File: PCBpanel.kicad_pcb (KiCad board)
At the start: 2 copper layers, 100 x 100.2 mm, 93 parts, among them P1 CONN_01X05, P1 CONN_01X13, P1 CONN_buzz, P2 CONN_01X03, P2 CONN_01X09, P3 CONN_01X04, P3 CONN_01X09, P3 CONN_01X13, P4 CONN_01X02, Q1 BSS138, Q1 BSS84, Q1 NPN, Q2 BSS138, SW1 SW_PUSH, U1 ESP-12E, U1 GY-NEO6MV2, U2 AP1117, U3 ESP8266_THING, U4 MPU6050, U5 NVSRAM, U6 BMP180, U7 HTU21D

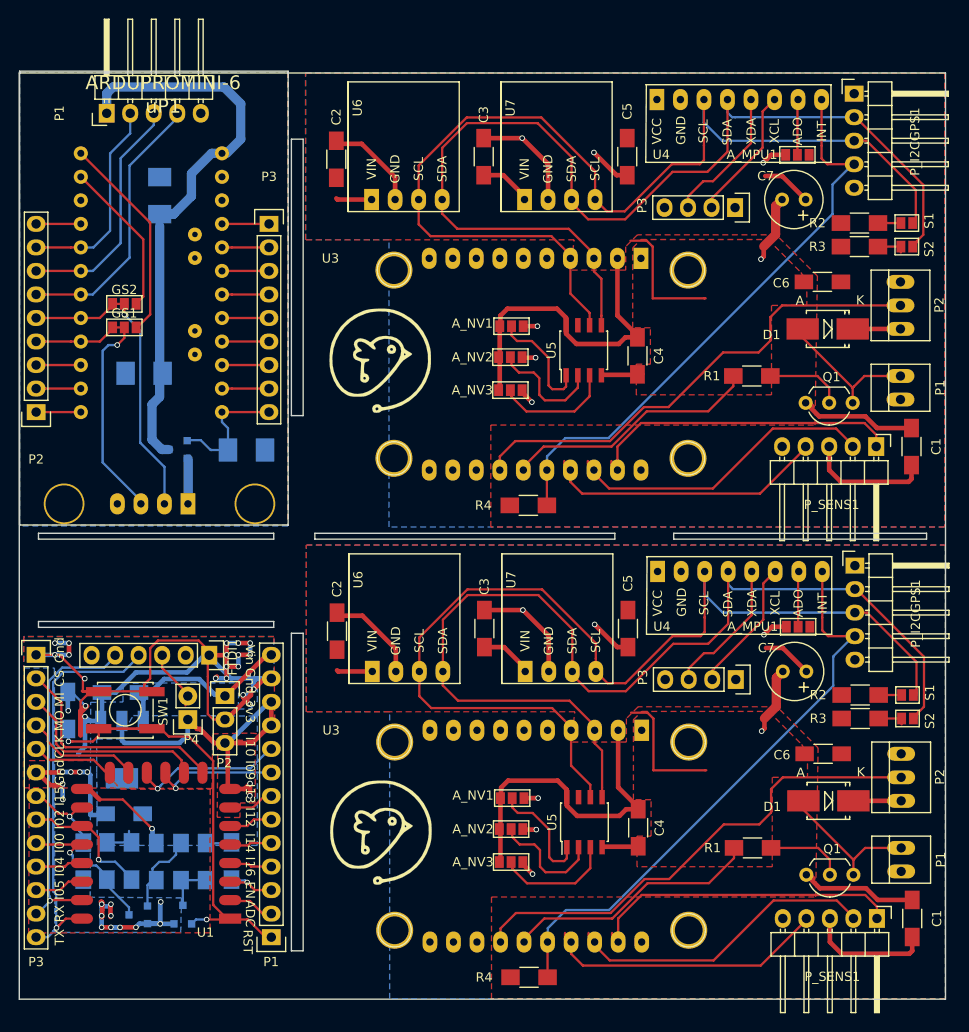
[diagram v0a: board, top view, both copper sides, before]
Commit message: alfa prototype
updated for first pcb prototype
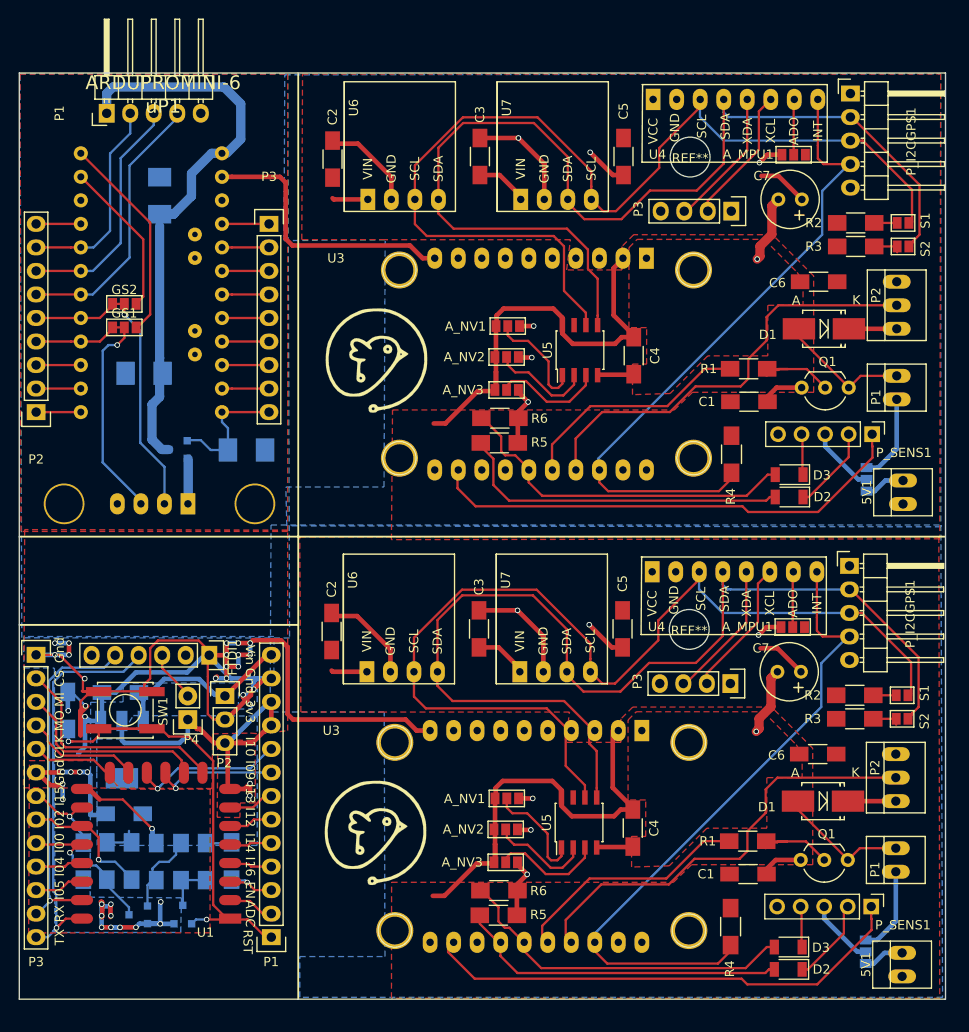
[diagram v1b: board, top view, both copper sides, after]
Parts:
- removed the A_MPU1 at (134.0, 58.8)
- removed the A_MPU1 at (134.1, 109.8)
- removed the A_NV1 at (103.1, 77.3)
- removed the A_NV1 at (103.2, 128.3)
- removed the A_NV2 at (103.0, 80.7)
- removed the A_NV2 at (103.1, 131.6)
- removed the A_NV3 at (103.0, 84.2)
- removed the A_NV3 at (103.1, 135.2)
- removed the C1 at (146.3, 90.3)
- removed the C1 at (146.4, 141.3)
- removed the C2 at (84.2, 59.3)
- removed the C2 at (84.3, 110.3)
- removed the C3 at (100.1, 59.0)
- removed the C3 at (100.2, 110.0)
- removed the C4 at (116.7, 80.5)
- removed the C4 at (116.8, 131.5)
- removed the C5 at (115.6, 59.0)
- removed the C5 at (115.7, 110.0)
- removed the C6 at (136.7, 72.6)
- removed the C6 at (136.8, 123.5)
- removed the C7 at (134.9, 63.7)
- removed the C7 at (135.0, 114.6)
- removed the D1 at (137.3, 77.6)
- removed the D1 at (137.4, 128.6)
- removed G*** (x2): LOGO, Adem_Kicad_logos:adem_logo
- removed G*** (x2): LOGO, Adem_Kicad_logos:adem_logo-txt_17_B_silk
- removed the P1 at (145.1, 84.0)
- removed the P1 at (145.2, 134.9)
- removed the P2 at (145.1, 75.1)
- removed the P2 at (145.2, 126.0)
- removed the P3 at (127.3, 64.5)
- removed the P3 at (127.4, 115.5)
- removed the P_I2CGPS1 at (140.1, 52.2)
- removed the P_I2CGPS1 at (140.2, 103.2)
- removed the P_SENS1 at (142.5, 90.3)
- removed the P_SENS1 at (142.6, 141.3)
- removed the Q1 at (140.0, 85.6)
- removed the Q1 at (140.1, 136.6)
- removed the R1 at (129.1, 82.7)
- removed the R1 at (129.2, 133.7)
- removed the R2 at (140.7, 66.2)
- removed the R2 at (140.8, 117.2)
- removed the R3 at (140.7, 68.7)
- removed the R3 at (140.8, 119.7)
- removed the R4 at (105.0, 96.7)
- removed the R4 at (105.0, 147.6)
- removed the S1 at (145.8, 66.2)
- removed the S1 at (145.9, 117.2)
- removed the S2 at (145.8, 68.7)
- removed the S2 at (145.9, 119.7)
- removed the U3 at (133.6, 68.7)
- removed the U3 at (133.7, 119.7)
- removed the U4 at (137.6, 54.6)
- removed the U4 at (137.7, 105.5)
- removed the U5 at (110.9, 79.9)
- removed the U5 at (111.0, 130.9)
- removed the U6 at (85.5, 64.9)
- removed the U6 at (85.6, 115.9)
- removed the U7 at (102.0, 64.9)
- removed the U7 at (102.1, 115.9)
- added 5V1: 5V, Connect:PINHEAD1-2, F.Cu at (145.4, 96.5)
- added 5V1: 5V, Connect:PINHEAD1-2, F.Cu at (145.3, 147.5)
- added ?: , Adem_Kicad_logos:adem_logo, F.Cu at (88.5, 81.0)
- added ?: , Adem_Kicad_logos:adem_logo-txt_17_B_silk, F.Cu at (113.5, 81.8)
- added ?: , Adem_Kicad_logos:adem_logo, F.Cu at (88.4, 132.0)
- added ?: , Adem_Kicad_logos:adem_logo-txt_17_B_silk, F.Cu at (113.4, 132.8)
- added A_MPU1: GS_A0, Connect:GS3, F.Cu at (133.6, 58.8)
- added A_MPU1: GS_A0, Connect:GS3, F.Cu at (133.5, 109.8)
- added A_NV1: GS_A0, Connect:GS3, F.Cu at (102.7, 77.3)
- added A_NV1: GS_A0, Connect:GS3, F.Cu at (102.6, 128.3)
- added A_NV2: GS_A1, Connect:GS3, F.Cu at (102.6, 80.7)
- added A_NV2: GS_A1, Connect:GS3, F.Cu at (102.5, 131.7)
- added A_NV3: GS_A2, Connect:GS3, F.Cu at (102.6, 84.2)
- added A_NV3: GS_A2, Connect:GS3, F.Cu at (102.5, 135.2)
- added C1: C, Capacitors_SMD:C_1206_HandSoldering, F.Cu at (128.8, 85.5)
- added C1: C, Capacitors_SMD:C_1206_HandSoldering, F.Cu at (128.7, 136.5)
- added C2: C, Capacitors_SMD:C_1206_HandSoldering, F.Cu at (83.8, 59.3)
- added C2: C, Capacitors_SMD:C_1206_HandSoldering, F.Cu at (83.7, 110.3)
- added C3: C, Capacitors_SMD:C_1206_HandSoldering, F.Cu at (99.7, 59.0)
- added C3: C, Capacitors_SMD:C_1206_HandSoldering, F.Cu at (99.6, 110.0)
- added C4: C, Capacitors_SMD:C_1206_HandSoldering, F.Cu at (116.3, 80.5)
- added C4: C, Capacitors_SMD:C_1206_HandSoldering, F.Cu at (116.2, 131.5)
- added C5: C, Capacitors_SMD:C_1206_HandSoldering, F.Cu at (115.2, 59.0)
- added C5: C, Capacitors_SMD:C_1206_HandSoldering, F.Cu at (115.1, 110.0)
- added C6: C, Capacitors_SMD:C_1206_HandSoldering, F.Cu at (136.3, 72.5)
- added C6: C, Capacitors_SMD:C_1206_HandSoldering, F.Cu at (136.2, 123.5)
- added C7: CP, Capacitors_Elko_ThroughHole:Elko_vert_11.2x6.3mm_RM2.5, F.Cu at (134.5, 63.6)
- added C7: CP, Capacitors_Elko_ThroughHole:Elko_vert_11.2x6.3mm_RM2.5, F.Cu at (134.4, 114.7)
- added D1: DIODE, Diodes_SMD:SMB_Handsoldering, F.Cu at (136.9, 77.6)
- added D1: DIODE, Diodes_SMD:SMB_Handsoldering, F.Cu at (136.8, 128.6)
- added D2: 1V8, Diodes_SMD:D_1206, F.Cu at (133.1, 95.8)
- added D2: 1V8, Diodes_SMD:D_1206, F.Cu at (133.0, 146.8)
- added D3: 1V8, Diodes_SMD:D_1206, F.Cu at (133.1, 93.4)
- added D3: 1V8, Diodes_SMD:D_1206, F.Cu at (133.0, 144.4)
- added P1: CONN_buzz, Connect:PINHEAD1-2, F.Cu at (144.7, 84.0)
- added P1: CONN_buzz, Connect:PINHEAD1-2, F.Cu at (144.6, 135.0)
- added P2: CONN_01X03, Connect:PINHEAD1-3, F.Cu at (144.7, 75.1)
- added P2: CONN_01X03, Connect:PINHEAD1-3, F.Cu at (144.6, 126.1)
- added P3: CONN_01X04, Pin_Headers:Pin_Header_Straight_1x04, F.Cu at (126.9, 64.9)
- added P3: CONN_01X04, Pin_Headers:Pin_Header_Straight_1x04, F.Cu at (126.8, 115.9)
- added P_I2CGPS1: CONN_01X05, Pin_Headers:Pin_Header_Angled_1x05, F.Cu at (139.7, 52.2)
- added P_I2CGPS1: CONN_01X05, Pin_Headers:Pin_Header_Angled_1x05, F.Cu at (139.6, 103.2)
- added P_SENS1: CONN_01X05, Pin_Headers:Pin_Header_Straight_1x05_Pitch2.54mm, F.Cu at (142.1, 89.0)
- added P_SENS1: CONN_01X05, Pin_Headers:Pin_Header_Straight_1x05_Pitch2.54mm, F.Cu at (142.0, 140.0)
- added Q1: NPN, TO_SOT_Packages_THT:TO-92_Inline_Wide, F.Cu at (139.5, 84.0)
- added Q1: NPN, TO_SOT_Packages_THT:TO-92_Inline_Wide, F.Cu at (139.4, 135.0)
- added R1: R, Resistors_SMD:R_1206_HandSoldering, F.Cu at (128.7, 81.9)
- added R1: R, Resistors_SMD:R_1206_HandSoldering, F.Cu at (128.6, 132.9)
- added R2: R, Resistors_SMD:R_1206_HandSoldering, F.Cu at (140.3, 66.2)
- added R2: R, Resistors_SMD:R_1206_HandSoldering, F.Cu at (140.2, 117.2)
- added R3: R, Resistors_SMD:R_1206_HandSoldering, F.Cu at (140.3, 68.7)
- added R3: R, Resistors_SMD:R_1206_HandSoldering, F.Cu at (140.2, 119.7)
- added R4: R, Resistors_SMD:R_1206_HandSoldering, F.Cu at (126.9, 91.2)
- added R4: R, Resistors_SMD:R_1206_HandSoldering, F.Cu at (126.8, 142.2)
- added R5: 10K, Resistors_SMD:R_1206_HandSoldering, F.Cu at (101.8, 89.9)
- added R5: 10K, Resistors_SMD:R_1206_HandSoldering, F.Cu at (101.7, 140.9)
- added R6: 10K, Resistors_SMD:R_1206_HandSoldering, F.Cu at (101.9, 87.3)
- added R6: 10K, Resistors_SMD:R_1206_HandSoldering, F.Cu at (101.8, 138.3)
- added REF**: MountingHole_4.3mm_M4, Mounting_Holes:MountingHole_4.3mm_M4, F.Cu at (122.4, 59.1)
- added REF**: MountingHole_4.3mm_M4, Mounting_Holes:MountingHole_4.3mm_M4, F.Cu at (122.3, 110.1)
- added S1: S1, Connect:GS2, F.Cu at (145.4, 66.2)
- added S1: S1, Connect:GS2, F.Cu at (145.3, 117.2)
- added S2: S2, Connect:GS2, F.Cu at (145.4, 68.7)
- added S2: S2, Connect:GS2, F.Cu at (145.3, 119.7)
- added U3: ESP8266_THING, ADEM:ESP8266_THING, F.Cu at (134.2, 68.7)
- added U3: ESP8266_THING, ADEM:ESP8266_THING, F.Cu at (133.7, 119.7)
- added U4: MPU6050, ADEM:MPU6050_angled, F.Cu at (137.2, 54.6)
- added U4: MPU6050, ADEM:MPU6050_angled, F.Cu at (137.1, 105.6)
- added U5: NVSRAM, Housings_SOIC:SOIC-8_3.9x4.9mm_Pitch1.27mm, F.Cu at (110.5, 79.9)
- added U5: NVSRAM, Housings_SOIC:SOIC-8_3.9x4.9mm_Pitch1.27mm, F.Cu at (110.4, 130.9)
- added U6: BMP180, ADEM:BMP180, F.Cu at (85.0, 115.9)
- added U6: BMP180, ADEM:BMP180, F.Cu at (85.1, 64.9)
- added U7: HTU21D, ADEM:HTU21D, F.Cu at (101.6, 64.9)
- added U7: HTU21D, ADEM:HTU21D, F.Cu at (101.5, 115.9)
- added VCC_SEL1: GS_VCC, Connect:GS3, B.Cu at (141.5, 93.9)
- added VCC_SEL1: GS_VCC, Connect:GS3, B.Cu at (141.4, 144.9)
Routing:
- net (no net): track 128.0 -> 300.0 mm
- net P25_SENS_SHFT: track 0.00 -> 75.4 mm
- net P10_SENS_SHFT: track 0.00 -> 72.7 mm
- net P25_SENS: track 60.2 -> 8.82 mm
- net GND: track 292.0 -> 341.8 mm
- net P10_SENS: track 65.8 -> 18.6 mm
- net A_SENSOR: track 67.4 -> 106.0 mm
- net INT: track 157.2 -> 172.5 mm
- net Net-(P_SENS1-Pad3): track 0.00 -> 14.4 mm
- net VCC: track 205.8 -> 218.0 mm
- net NEO_PXL: track 105.9 -> 94.3 mm
- net Net-(5V1-Pad2): track 0.00 -> 10.3 mm
- net Net-(R3-Pad1): track 0.00 -> 5.05 mm
- net Net-(GS2-Pad2): track 5.05 -> 0.00 mm
- net BUZZ: track 56.2 -> 51.2 mm
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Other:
- board size 100 x 100.2 mm -> 100 x 100 mm
- net class POWER added: clearance 0.2, trace_width 0.5, via_dia 0.6, via_drill 0.4
- board text added: "www.ik-adem.be github.com/timelab/ADEM github.com/timelab/ADEM-hardware"
- board text removed: "github.com/timelab/ADEM-hardware github.com/timelab/ADEM www.ik-adem.be"
